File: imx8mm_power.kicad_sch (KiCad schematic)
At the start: 58 parts, among them U1 MIMX8MM6DVTLZAA

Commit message: most of routing done
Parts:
- removed C19: 1uF, qsbc:C_0201_0603Metric, symbol Device:C
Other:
- moved on the sheet: C10, C14, C4
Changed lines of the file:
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@@
   (junction (at 337.82 186.69) (diameter 0) (color 0 0 0 0)
   )
-  (junction (at 76.2 175.26) (diameter 0) (color 0 0 0 0)
+  (junction (at 88.9 175.26) (diameter 0) (color 0 0 0 0)
   )
   (junction (at 99.06 91.44) (diameter 0) (color 0 0 0 0)
@@
   (junction (at 158.75 121.92) (diameter 0) (color 0 0 0 0)
   )
-  (junction (at 100.33 162.56) (diameter 0) (color 0 0 0 0)
-  )
   (junction (at 393.7 118.11) (diameter 0) (color 0 0 0 0)
   )
@@
   (junction (at 337.82 151.13) (diameter 0) (color 0 0 0 0)
   )
-  (junction (at 100.33 175.26) (diameter 0) (color 0 0 0 0)
-  )
   (junction (at 158.75 223.52) (diameter 0) (color 0 0 0 0)
   )
-  (junction (at 76.2 162.56) (diameter 0) (color 0 0 0 0)
+  (junction (at 88.9 162.56) (diameter 0) (color 0 0 0 0)
   )
   (junction (at 158.75 116.84) (diameter 0) (color 0 0 0 0)
@@
   (junction (at 214.63 78.74) (diameter 0) (color 0 0 0 0)
   )
-  (junction (at 63.5 162.56) (diameter 0) (color 0 0 0 0)
+  (junction (at 77.47 162.56) (diameter 0) (color 0 0 0 0)
   )
   (junction (at 87.63 91.44) (diameter 0) (color 0 0 0 0)
@@
   (junction (at 158.75 218.44) (diameter 0) (color 0 0 0 0)
   )
-  (junction (at 88.9 175.26) (diameter 0) (color 0 0 0 0)
+  (junction (at 100.33 175.26) (diameter 0) (color 0 0 0 0)
   )
   (junction (at 111.76 175.26) (diameter 0) (color 0 0 0 0)
@@
   (junction (at 76.2 104.14) (diameter 0) (color 0 0 0 0)
   )
-  (junction (at 88.9 162.56) (diameter 0) (color 0 0 0 0)
+  (junction (at 100.33 162.56) (diameter 0) (color 0 0 0 0)
   )
   (junction (at 156.21 190.5) (diameter 0) (color 0 0 0 0)
@@
     (stroke (width 0) (type default) (color 0 0 0 0))
   )
-  (wire (pts (xy 88.9 162.56) (xy 76.2 162.56))
+  (wire (pts (xy 100.33 162.56) (xy 88.9 162.56))
     (stroke (width 0) (type default) (color 0 0 0 0))
   )
@@
     (stroke (width 0) (type default) (color 0 0 0 0))
   )
-  (wire (pts (xy 88.9 175.26) (xy 100.33 175.26))
-    (stroke (width 0) (type default) (color 0 0 0 0))
-  )
   (wire (pts (xy 245.11 254) (xy 259.08 254))
     (stroke (width 0) (type default) (color 0 0 0 0))
@@
     (stroke (width 0) (type default) (color 0 0 0 0))
   )
-  (wire (pts (xy 88.9 172.72) (xy 88.9 175.26))
+  (wire (pts (xy 100.33 172.72) (xy 100.33 175.26))
     (stroke (width 0) (type default) (color 0 0 0 0))
   )
@@
     (stroke (width 0) (type default) (color 0 0 0 0))
   )
-  (wire (pts (xy 40.64 162.56) (xy 63.5 162.56))
+  (wire (pts (xy 54.61 162.56) (xy 77.47 162.56))
     (stroke (width 0) (type default) (color 0 0 0 0))
   )
@@
     (stroke (width 0) (type default) (color 0 0 0 0))
   )
-  (wire (pts (xy 100.33 172.72) (xy 100.33 175.26))
-    (stroke (width 0) (type default) (color 0 0 0 0))
-  )
   (wire (pts (xy 234.95 157.48) (xy 247.65 157.48))
     (stroke (width 0) (type default) (color 0 0 0 0))
@@
     (stroke (width 0) (type default) (color 0 0 0 0))
   )
-  (wire (pts (xy 100.33 162.56) (xy 88.9 162.56))
+  (wire (pts (xy 100.33 162.56) (xy 111.76 162.56))
     (stroke (width 0) (type default) (color 0 0 0 0))
   )
@@
     (stroke (width 0) (type default) (color 0 0 0 0))
   )
-  (wire (pts (xy 76.2 162.56) (xy 76.2 165.1))
+  (wire (pts (xy 88.9 162.56) (xy 88.9 165.1))
     (stroke (width 0) (type default) (color 0 0 0 0))
   )
@@
     (stroke (width 0) (type default) (color 0 0 0 0))
   )
-  (wire (pts (xy 88.9 162.56) (xy 88.9 165.1))
+  (wire (pts (xy 100.33 162.56) (xy 100.33 165.1))
     (stroke (width 0) (type default) (color 0 0 0 0))
   )
@@
     (stroke (width 0) (type default) (color 0 0 0 0))
   )
-  (wire (pts (xy 76.2 162.56) (xy 63.5 162.56))
+  (wire (pts (xy 88.9 162.56) (xy 77.47 162.56))
     (stroke (width 0) (type default) (color 0 0 0 0))
   )
@@
     (stroke (width 0) (type default) (color 0 0 0 0))
   )
-  (wire (pts (xy 63.5 162.56) (xy 63.5 165.1))
+  (wire (pts (xy 77.47 162.56) (xy 77.47 165.1))
     (stroke (width 0) (type default) (color 0 0 0 0))
   )
@@
     (stroke (width 0) (type default) (color 0 0 0 0))
   )
-  (wire (pts (xy 76.2 172.72) (xy 76.2 175.26))
+  (wire (pts (xy 88.9 172.72) (xy 88.9 175.26))
     (stroke (width 0) (type default) (color 0 0 0 0))
   )
@@
     (stroke (width 0) (type default) (color 0 0 0 0))
   )
-  (wire (pts (xy 76.2 175.26) (xy 88.9 175.26))
+  (wire (pts (xy 88.9 175.26) (xy 100.33 175.26))
     (stroke (width 0) (type default) (color 0 0 0 0))
   )
@@
     (stroke (width 0) (type default) (color 0 0 0 0))
   )
-  (wire (pts (xy 63.5 175.26) (xy 63.5 172.72))
+  (wire (pts (xy 77.47 175.26) (xy 77.47 172.72))
     (stroke (width 0) (type default) (color 0 0 0 0))
   )
@@
     (stroke (width 0) (type default) (color 0 0 0 0))
   )
-  (wire (pts (xy 111.76 162.56) (xy 100.33 162.56))
-    (stroke (width 0) (type default) (color 0 0 0 0))
-  )
   (wire (pts (xy 393.7 196.85) (xy 391.16 196.85))
     (stroke (width 0) (type default) (color 0 0 0 0))
@@
     (stroke (width 0) (type default) (color 0 0 0 0))
   )
-  (wire (pts (xy 63.5 175.26) (xy 76.2 175.26))
+  (wire (pts (xy 77.47 175.26) (xy 88.9 175.26))
     (stroke (width 0) (type default) (color 0 0 0 0))
   )
@@
     (stroke (width 0) (type default) (color 0 0 0 0))
   )
-  (wire (pts (xy 100.33 162.56) (xy 100.33 165.1))
-    (stroke (width 0) (type default) (color 0 0 0 0))
-  )
   (wire (pts (xy 337.82 120.65) (xy 340.36 120.65))
     (stroke (width 0) (type default) (color 0 0 0 0))
@@
     (effects (font (size 1.27 1.27)) (justify left bottom))
   )
-  (label "VDD_DRAM_xPU_0.9V" (at 40.64 162.56 0)
+  (label "VDD_DRAM_xPU_0.9V" (at 54.61 162.56 0)
     (effects (font (size 1.27 1.27)) (justify left bottom))
   )
@@
     (pin "1")
   )
-  (symbol (lib_id "Device:C") (at 76.2 168.91 0) (unit 1)
+  (symbol (lib_id "Device:C") (at 88.9 168.91 0) (unit 1)
     (in_bom yes) (on_board yes)
-    (property "Reference" "C10" (id 0) (at 80.01 167.6399 0)
+    (property "Reference" "C10" (id 0) (at 92.71 167.6399 0)
       (effects (font (size 1.27 1.27)) (justify left))
     )
-    (property "Value" "10uF" (id 1) (at 80.01 170.1799 0)
+    (property "Value" "10uF" (id 1) (at 92.71 170.1799 0)
       (effects (font (size 1.27 1.27)) (justify left))
     )
-    (property "Footprint" "qsbc:C_0402_1005Metric" (id 2) (at 77.1652 172.72 0)
+    (property "Footprint" "qsbc:C_0402_1005Metric" (id 2) (at 89.8652 172.72 0)
       (effects (font (size 1.27 1.27)) hide)
     )
-    (property "Datasheet" "~" (id 3) (at 76.2 168.91 0)
+    (property "Datasheet" "~" (id 3) (at 88.9 168.91 0)
       (effects (font (size 1.27 1.27)) hide)
     )
-    (property "Rating" "6.3V/20%" (id 4) (at 82.55 172.72 0)
+    (property "Rating" "6.3V/20%" (id 4) (at 95.25 172.72 0)
       (effects (font (size 0.762 0.762)))
     )
@@
     (pin "2")
   )
-  (symbol (lib_id "Device:C") (at 63.5 168.91 0) (unit 1)
+  (symbol (lib_id "Device:C") (at 77.47 168.91 0) (unit 1)
     (in_bom yes) (on_board yes)
-    (property "Reference" "C4" (id 0) (at 67.31 167.6399 0)
+    (property "Reference" "C4" (id 0) (at 81.28 167.6399 0)
       (effects (font (size 1.27 1.27)) (justify left))
     )
-    (property "Value" "10uF" (id 1) (at 67.31 170.1799 0)
+    (property "Value" "10uF" (id 1) (at 81.28 170.1799 0)
       (effects (font (size 1.27 1.27)) (justify left))
     )
-    (property "Footprint" "qsbc:C_0402_1005Metric" (id 2) (at 64.4652 172.72 0)
+    (property "Footprint" "qsbc:C_0402_1005Metric" (id 2) (at 78.4352 172.72 0)
       (effects (font (size 1.27 1.27)) hide)
     )
-    (property "Datasheet" "~" (id 3) (at 63.5 168.91 0)
+    (property "Datasheet" "~" (id 3) (at 77.47 168.91 0)
       (effects (font (size 1.27 1.27)) hide)
     )
-    (property "Rating" "6.3V/20%" (id 4) (at 69.85 172.72 0)
+    (property "Rating" "6.3V/20%" (id 4) (at 83.82 172.72 0)
       (effects (font (size 0.762 0.762)))
     )
@@
     (pin "2")
   )
-  (symbol (lib_id "Device:C") (at 88.9 168.91 0) (unit 1)
+  (symbol (lib_id "Device:C") (at 100.33 168.91 0) (unit 1)
     (in_bom yes) (on_board yes)
-    (property "Reference" "C14" (id 0) (at 92.71 167.6399 0)
+    (property "Reference" "C14" (id 0) (at 104.14 167.6399 0)
       (effects (font (size 1.27 1.27)) (justify left))
     )
-    (property "Value" "1uF" (id 1) (at 92.71 170.1799 0)
+    (property "Value" "1uF" (id 1) (at 104.14 170.1799 0)
       (effects (font (size 1.27 1.27)) (justify left))
     )
-    (property "Footprint" "qsbc:C_0201_0603Metric" (id 2) (at 89.8652 172.72 0)
+    (property "Footprint" "qsbc:C_0201_0603Metric" (id 2) (at 101.2952 172.72 0)
       (effects (font (size 1.27 1.27)) hide)
     )
-    (property "Datasheet" "~" (id 3) (at 88.9 168.91 0)
+    (property "Datasheet" "~" (id 3) (at 100.33 168.91 0)
       (effects (font (size 1.27 1.27)) hide)
     )
-    (property "Rating" "6.3V/20%" (id 4) (at 95.25 172.72 0)
+    (property "Rating" "6.3V/20%" (id 4) (at 106.68 172.72 0)
       (effects (font (size 0.762 0.762)))
     )
@@
     (pin "1")
   )
-  (symbol (lib_id "Device:C") (at 100.33 168.91 0) (unit 1)
-    (in_bom yes) (on_board yes)
-    (property "Reference" "C19" (id 0) (at 104.14 167.6399 0)
-      (effects (font (size 1.27 1.27)) (justify left))
-    )
-    (property "Value" "1uF" (id 1) (at 104.14 170.1799 0)
-      (effects (font (size 1.27 1.27)) (justify left))
-    )
-    (property "Footprint" "qsbc:C_0201_0603Metric" (id 2) (at 101.2952 172.72 0)
-      (effects (font (size 1.27 1.27)) hide)
-    )
-    (property "Datasheet" "~" (id 3) (at 100.33 168.91 0)
-      (effects (font (size 1.27 1.27)) hide)
-    )
-    (property "Rating" "6.3V/20%" (id 4) (at 106.68 172.72 0)
-      (effects (font (size 0.762 0.762)))
-    )
-    (pin "1")
-    (pin "2")
-  )
 )

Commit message: bom work, change uart level shifter and m.2 socket
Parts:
- C1, C12, C13, C14, C15, C17, C18, C20, C21, C22, C23, C24, C25, C26, C27, C28, C29, C30, C31, C32, C6, C8, C9: MPN (none) -> GRM033R60J105MEA2D
- C10, C11, C2, C3, C35, C38, C4, C41, C5: MPN (none) -> GRM155R60J106ME44D
- C16, C33, C36, C37, C40, C42, C43, C44, C45, C46, C47, C48, C49, C50, C51, C52, C53, C54, C55, C56, C57, C7: MPN (none) -> GRM033R60J224ME15D
- C34: MPN (none) -> GCM033R71C222KA55D
- C39: MPN (none) -> CL05A475MP5NRNC
- U1: MPN (none) -> MIMX8MM6DVTLZAA

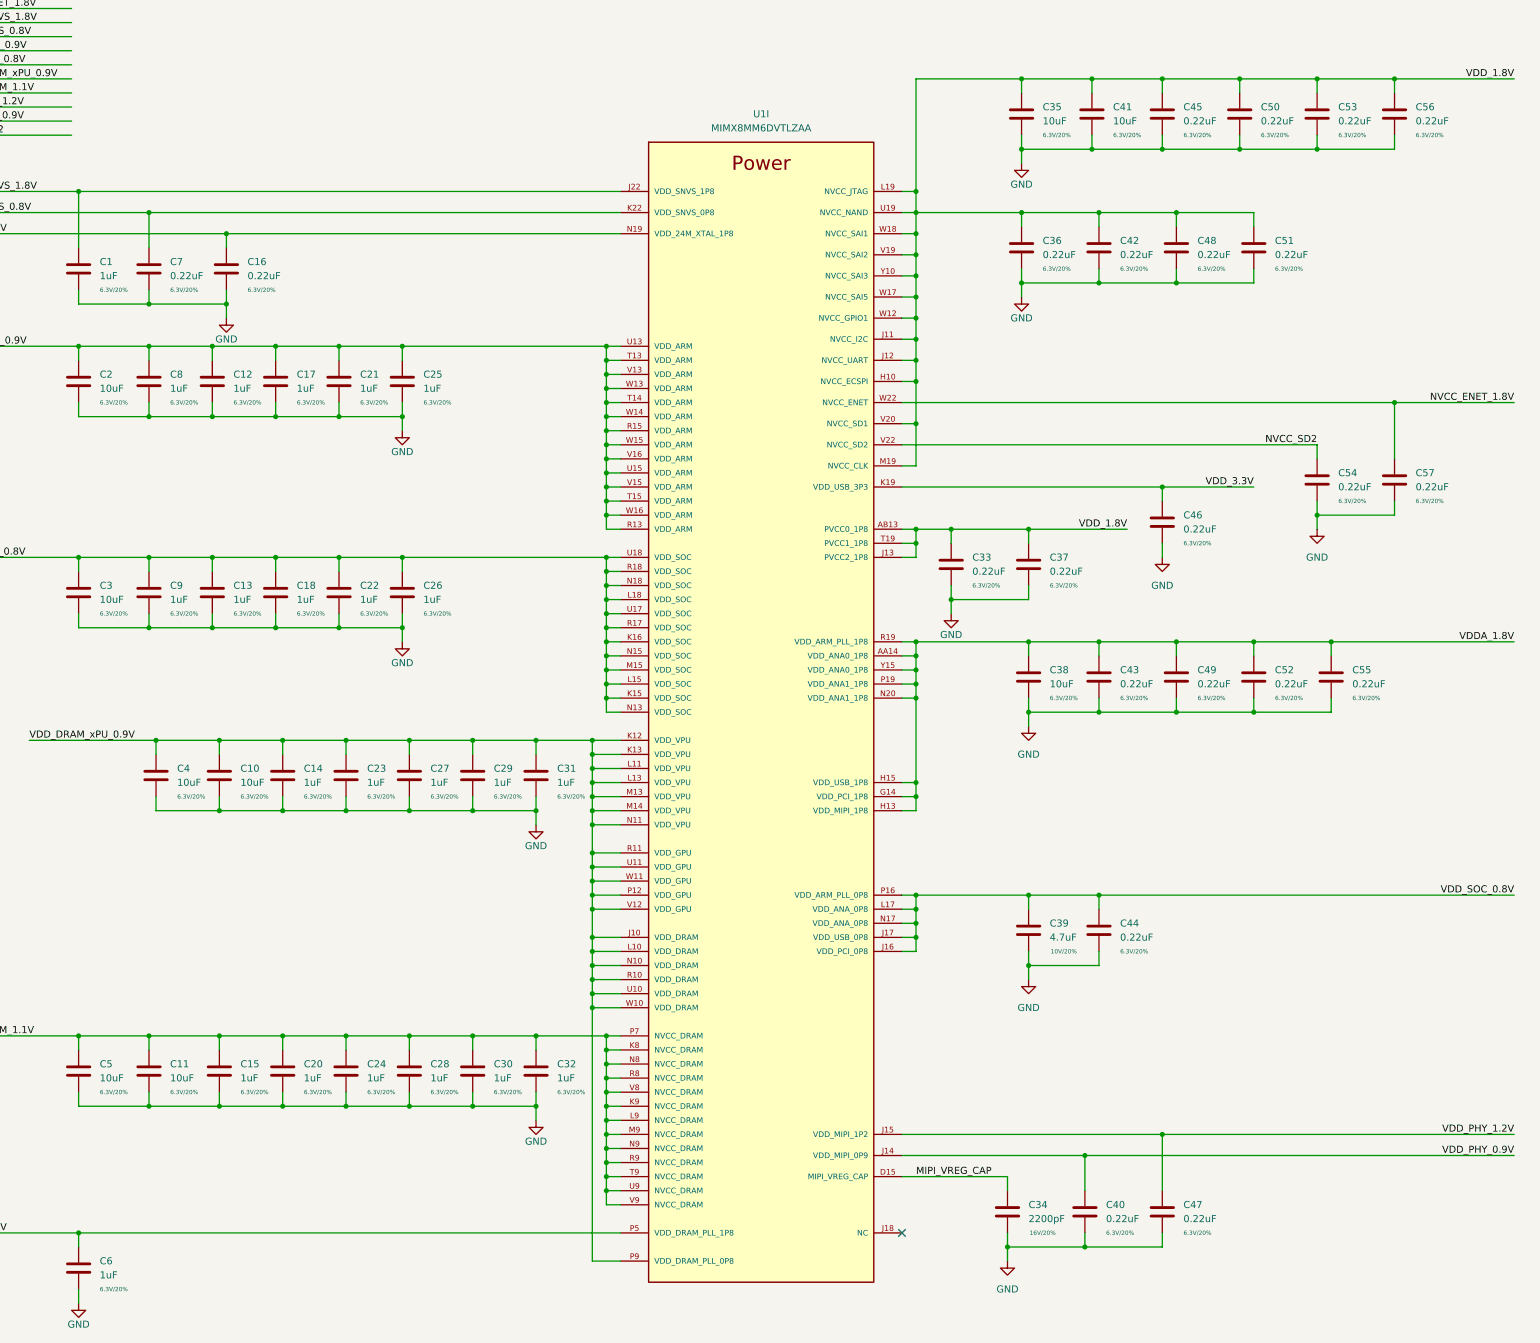
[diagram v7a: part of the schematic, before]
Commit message: ddr length matching work, misc cleanup
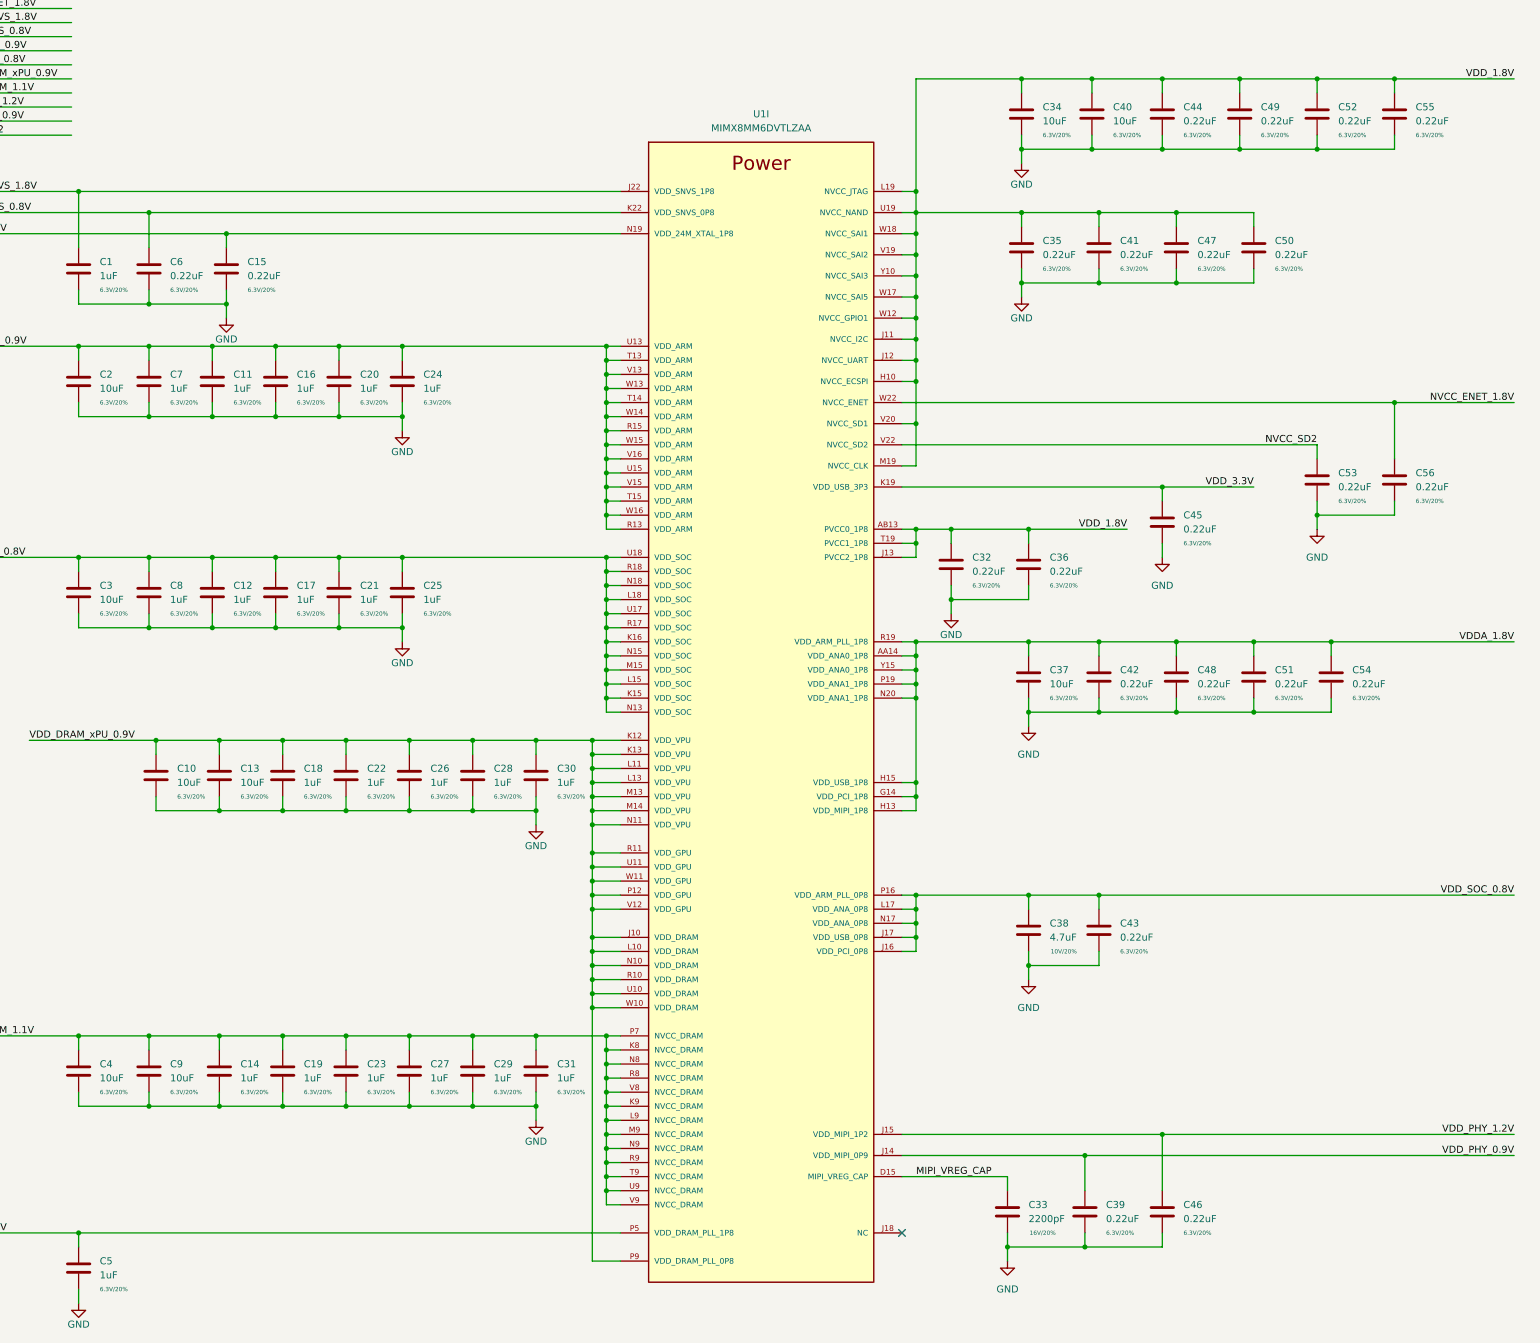
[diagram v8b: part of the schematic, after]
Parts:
- renumbered C4 to C10, C12 to C11, C13 to C12, C10 to C13, C15 to C14, C16 to C15, C17 to C16, C18 to C17, C14 to C18, C20 to C19, C21 to C20, C22 to C21, C23 to C22, C24 to C23, C25 to C24, C26 to C25, C27 to C26, C28 to C27, C29 to C28, C30 to C29, C31 to C30, C32 to C31, C33 to C32, C34 to C33, C35 to C34, C36 to C35, C37 to C36, C38 to C37, C39 to C38, C40 to C39, C5 to C4, C41 to C40, C42 to C41, C43 to C42, C44 to C43, C45 to C44, C46 to C45, C47 to C46, C48 to C47, C49 to C48, C50 to C49, C6 to C5, C51 to C50, C52 to C51, C53 to C52, C54 to C53, C55 to C54, C56 to C55, C57 to C56, C7 to C6, C8 to C7, C9 to C8, C11 to C9
